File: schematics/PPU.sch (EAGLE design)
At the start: 51 parts, among them Q1 KIA431, Q2 KN2222A, Q3 2SC945, U12 UM6618, U13 53.693175MHz, U3 UM70C188, U4 KA2195D, U5 UM611024, U6 UM611024

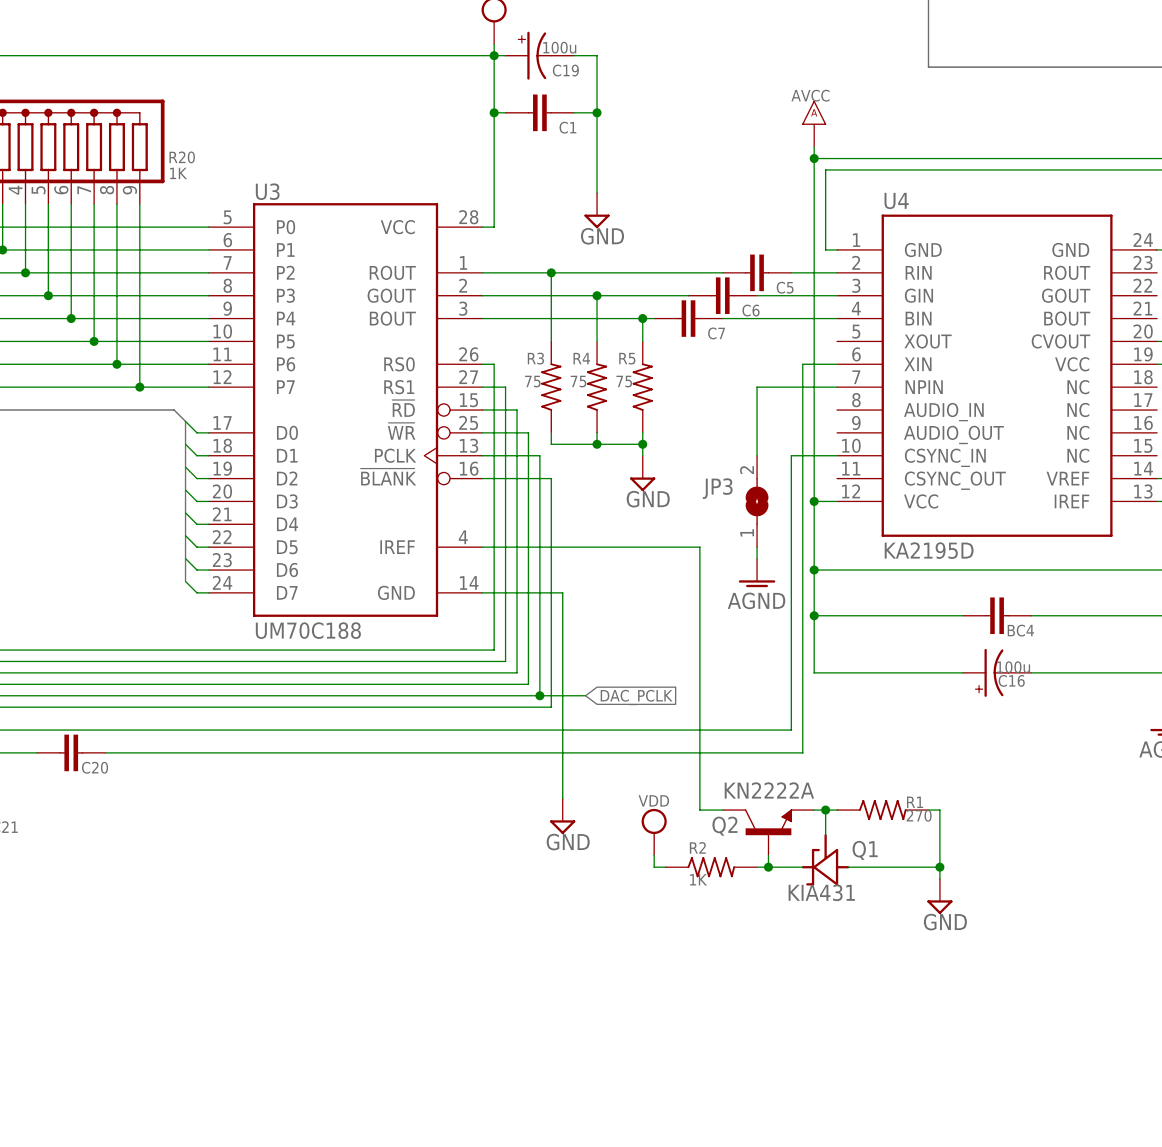
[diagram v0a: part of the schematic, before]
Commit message: Correct connections around Q1 and Q2.
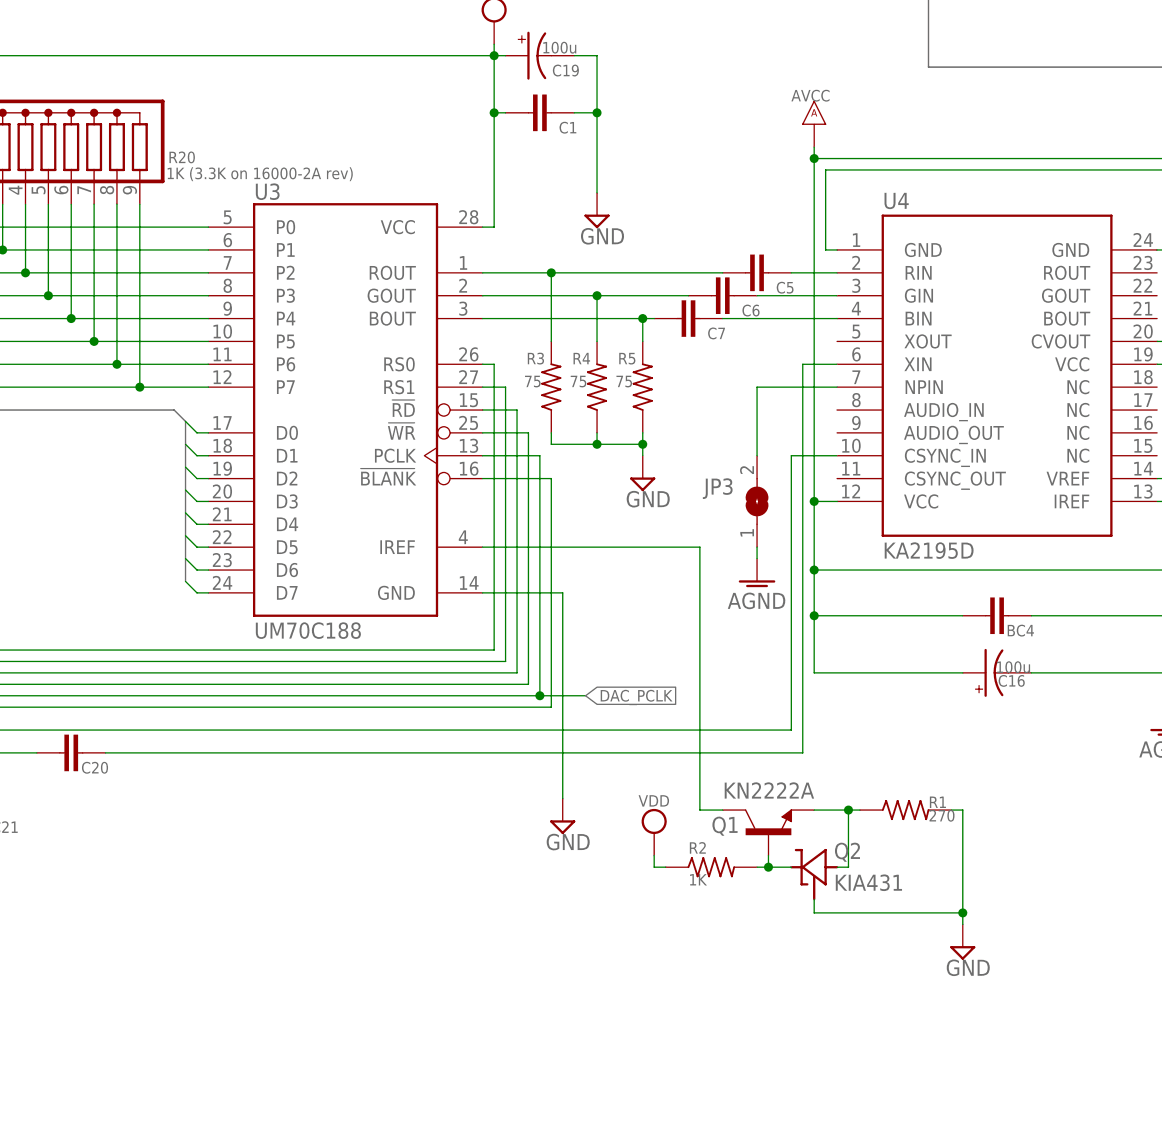
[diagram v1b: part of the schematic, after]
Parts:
- Q1: value KIA431 -> KN2222A; device acan:KIA431 -> acan:KN2222A
- Q2: value KN2222A -> KIA431; device acan:KN2222A -> acan:KIA431
- R20: value 1K -> 1K (3.3K on 16000-2A rev)
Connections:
- net GND: now also Q2.R; no longer Q1.A
- net N$29: now also Q1.C; no longer Q2.C
- net N$30: now also Q1.B, Q2.C; no longer Q1.C, Q2.B
- net N$32: now also Q1.E, Q2.A; no longer Q1.R, Q2.E
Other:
- moved on the sheet: R1
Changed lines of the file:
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@@
 <part name="BC5" library="rcl" library_urn="urn:adsk.eagle:library:334" deviceset="C-EU" device="C0805" package3d_urn="urn:adsk.eagle:package:23617/2"/>
 <part name="BC6" library="rcl" library_urn="urn:adsk.eagle:library:334" deviceset="C-EU" device="C0805" package3d_urn="urn:adsk.eagle:package:23617/2"/>
-<part name="R20" library="resistor-sil" library_urn="urn:adsk.eagle:library:347" deviceset="G08R" device="" package3d_urn="urn:adsk.eagle:package:25282/1" value="1K"/>
+<part name="R20" library="resistor-sil" library_urn="urn:adsk.eagle:library:347" deviceset="G08R" device="" package3d_urn="urn:adsk.eagle:package:25282/1" value="1K (3.3K on 16000-2A rev)"/>
 <part name="C1" library="rcl" library_urn="urn:adsk.eagle:library:334" deviceset="C-EU" device="C0805" package3d_urn="urn:adsk.eagle:package:23617/2"/>
 <part name="R3" library="rcl" library_urn="urn:adsk.eagle:library:334" deviceset="R-US_" device="R0805" package3d_urn="urn:adsk.eagle:package:23553/2" value="75"/>
@@
 <part name="R12" library="rcl" library_urn="urn:adsk.eagle:library:334" deviceset="R-US_" device="R0805" package3d_urn="urn:adsk.eagle:package:23553/2" value="100"/>
 <part name="SUPPLY12" library="supply2" library_urn="urn:adsk.eagle:library:372" deviceset="GND" device=""/>
-<part name="Q1" library="acan" deviceset="KIA431" device="" package3d_urn="urn:adsk.eagle:package:29915/2" value="KIA431"/>
-<part name="Q2" library="acan" deviceset="KN2222A" device="" package3d_urn="urn:adsk.eagle:package:29915/2" value="KN2222A"/>
+<part name="Q2" library="acan" deviceset="KIA431" device="" package3d_urn="urn:adsk.eagle:package:29915/2" value="KIA431"/>
+<part name="Q1" library="acan" deviceset="KN2222A" device="" package3d_urn="urn:adsk.eagle:package:29915/2" value="KN2222A"/>
 <part name="SUPPLY13" library="supply2" library_urn="urn:adsk.eagle:library:372" deviceset="VDD" device=""/>
 <part name="R2" library="rcl" library_urn="urn:adsk.eagle:library:334" deviceset="R-US_" device="R0805" package3d_urn="urn:adsk.eagle:package:23553/2" value="1K"/>
@@
 <instance part="R20" gate="G$1" x="146.05" y="127" smashed="yes">
 <attribute name="NAME" x="159.893" y="126.492" size="1.27" layer="95" rot="R180" align="top-left"/>
-<attribute name="VALUE" x="158.877" y="125.984" size="1.27" layer="96" rot="R180"/>
+<attribute name="VALUE" x="156.591" y="124.714" size="1.27" layer="96"/>
 </instance>
 <instance part="C1" gate="G$1" x="199.39" y="132.08" smashed="yes" rot="MR90">
@@
 <attribute name="VALUE" x="290.195" y="93.345" size="1.778" layer="96"/>
 </instance>
-<instance part="Q1" gate="G$1" x="229.87" y="48.26" smashed="yes" rot="MR0">
-<attribute name="NAME" x="235.8644" y="49.3776" size="1.778" layer="95" rot="MR0"/>
-<attribute name="VALUE" x="233.3244" y="44.5262" size="1.778" layer="96" rot="MR0"/>
-</instance>
-<instance part="Q2" gate="G$1" x="223.52" y="52.07" smashed="yes" rot="R90">
+<instance part="Q2" gate="G$1" x="228.6" y="48.26" smashed="yes" rot="R180">
+<attribute name="NAME" x="230.7844" y="50.9524" size="1.778" layer="95" rot="MR180"/>
+<attribute name="VALUE" x="230.7844" y="45.6438" size="1.778" layer="96"/>
+</instance>
+<instance part="Q1" gate="G$1" x="223.52" y="52.07" smashed="yes" rot="R90">
 <attribute name="NAME" x="217.17" y="52.07" size="1.778" layer="95"/>
 <attribute name="VALUE" x="218.44" y="55.88" size="1.778" layer="96"/>
@@
 <attribute name="VALUE" x="214.63" y="46.228" size="1.27" layer="96"/>
 </instance>
-<instance part="R1" gate="G$1" x="236.22" y="54.61" smashed="yes">
-<attribute name="NAME" x="238.76" y="56.1086" size="1.27" layer="95" align="top-left"/>
-<attribute name="VALUE" x="238.76" y="54.61" size="1.27" layer="96" align="top-left"/>
-</instance>
-<instance part="SUPPLY14" gate="GND" x="242.57" y="44.45" smashed="yes">
-<attribute name="VALUE" x="240.665" y="41.275" size="1.778" layer="96"/>
+<instance part="R1" gate="G$1" x="238.76" y="54.61" smashed="yes">
+<attribute name="NAME" x="241.3" y="56.1086" size="1.27" layer="95" align="top-left"/>
+<attribute name="VALUE" x="241.3" y="54.61" size="1.27" layer="96" align="top-left"/>
+</instance>
+<instance part="SUPPLY14" gate="GND" x="245.11" y="39.37" smashed="yes">
+<attribute name="VALUE" x="243.205" y="36.195" size="1.778" layer="96"/>
 </instance>
 <instance part="C2" gate="G$1" x="295.91" y="171.45" smashed="yes" rot="MR90">
@@
 <segment>
 <pinref part="R1" gate="G$1" pin="2"/>
-<wire x1="241.3" y1="54.61" x2="242.57" y2="54.61" width="0.1524" layer="91"/>
-<wire x1="242.57" y1="54.61" x2="242.57" y2="48.26" width="0.1524" layer="91"/>
-<pinref part="Q1" gate="G$1" pin="A"/>
-<wire x1="242.57" y1="48.26" x2="232.41" y2="48.26" width="0.1524" layer="91"/>
-<wire x1="242.57" y1="48.26" x2="242.57" y2="46.99" width="0.1524" layer="91"/>
-<junction x="242.57" y="48.26"/>
+<wire x1="243.84" y1="54.61" x2="245.11" y2="54.61" width="0.1524" layer="91"/>
+<wire x1="245.11" y1="54.61" x2="245.11" y2="43.18" width="0.1524" layer="91"/>
 <pinref part="SUPPLY14" gate="GND" pin="GND"/>
+<pinref part="Q2" gate="G$1" pin="R"/>
+<wire x1="245.11" y1="43.18" x2="245.11" y2="41.91" width="0.1524" layer="91"/>
+<wire x1="228.6" y1="44.704" x2="228.6" y2="43.18" width="0.1524" layer="91"/>
+<wire x1="228.6" y1="43.18" x2="245.11" y2="43.18" width="0.1524" layer="91"/>
+<junction x="245.11" y="43.18"/>
 </segment>
 <segment>
@@
 <segment>
 <pinref part="U3" gate="G$1" pin="IREF"/>
-<pinref part="Q2" gate="G$1" pin="C"/>
+<pinref part="Q1" gate="G$1" pin="C"/>
 <wire x1="218.44" y1="54.61" x2="215.9" y2="54.61" width="0.1524" layer="91"/>
 <wire x1="215.9" y1="54.61" x2="215.9" y2="83.82" width="0.1524" layer="91"/>
@@
 <net name="N$30" class="0">
 <segment>
-<pinref part="Q2" gate="G$1" pin="B"/>
+<pinref part="Q1" gate="G$1" pin="B"/>
 <wire x1="223.52" y1="49.53" x2="223.52" y2="48.26" width="0.1524" layer="91"/>
-<pinref part="Q1" gate="G$1" pin="C"/>
-<wire x1="223.52" y1="48.26" x2="227.33" y2="48.26" width="0.1524" layer="91"/>
+<pinref part="Q2" gate="G$1" pin="C"/>
+<wire x1="223.52" y1="48.26" x2="226.06" y2="48.26" width="0.1524" layer="91"/>
 <pinref part="R2" gate="G$1" pin="2"/>
 <wire x1="222.25" y1="48.26" x2="223.52" y2="48.26" width="0.1524" layer="91"/>
@@
 <net name="N$32" class="0">
 <segment>
-<pinref part="Q2" gate="G$1" pin="E"/>
-<pinref part="Q1" gate="G$1" pin="R"/>
-<wire x1="229.87" y1="51.816" x2="229.87" y2="54.61" width="0.1524" layer="91"/>
-<wire x1="229.87" y1="54.61" x2="228.6" y2="54.61" width="0.1524" layer="91"/>
-<wire x1="229.87" y1="54.61" x2="231.14" y2="54.61" width="0.1524" layer="91"/>
-<junction x="229.87" y="54.61"/>
+<pinref part="Q1" gate="G$1" pin="E"/>
+<wire x1="228.6" y1="54.61" x2="232.41" y2="54.61" width="0.1524" layer="91"/>
 <pinref part="R1" gate="G$1" pin="1"/>
-</segment>
-</net>
+<pinref part="Q2" gate="G$1" pin="A"/>
+<wire x1="232.41" y1="54.61" x2="233.68" y2="54.61" width="0.1524" layer="91"/>
+<wire x1="231.14" y1="48.26" x2="232.41" y2="48.26" width="0.1524" layer="91"/>
+<wire x1="232.41" y1="48.26" x2="232.41" y2="54.61" width="0.1524" layer="91"/>
+<junction x="232.41" y="54.61"/>
+</segment>
+</net>
